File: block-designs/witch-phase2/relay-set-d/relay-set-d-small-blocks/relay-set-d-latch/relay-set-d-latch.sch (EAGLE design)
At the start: 53 parts, among them IC1 74LVC1G125DBV, IC10 741G175, IC11 74LVC1G06DBV, IC12 74LVC1G06DBV, IC13 74LVC1G06DBV, IC14 74LVC1G06DBV, IC15 74LVC1G06DBV, IC2 74LVC1G125DBV, IC3 74LVC1G125DBV, IC4 74LVC1G125DBV, IC5 74LVC1G125DBV, IC6 741G175, IC7 741G175, IC8 741G175, IC9 741G175, Q1 MMBT2907ALT1SMD, Q2 MMBT2907ALT1SMD

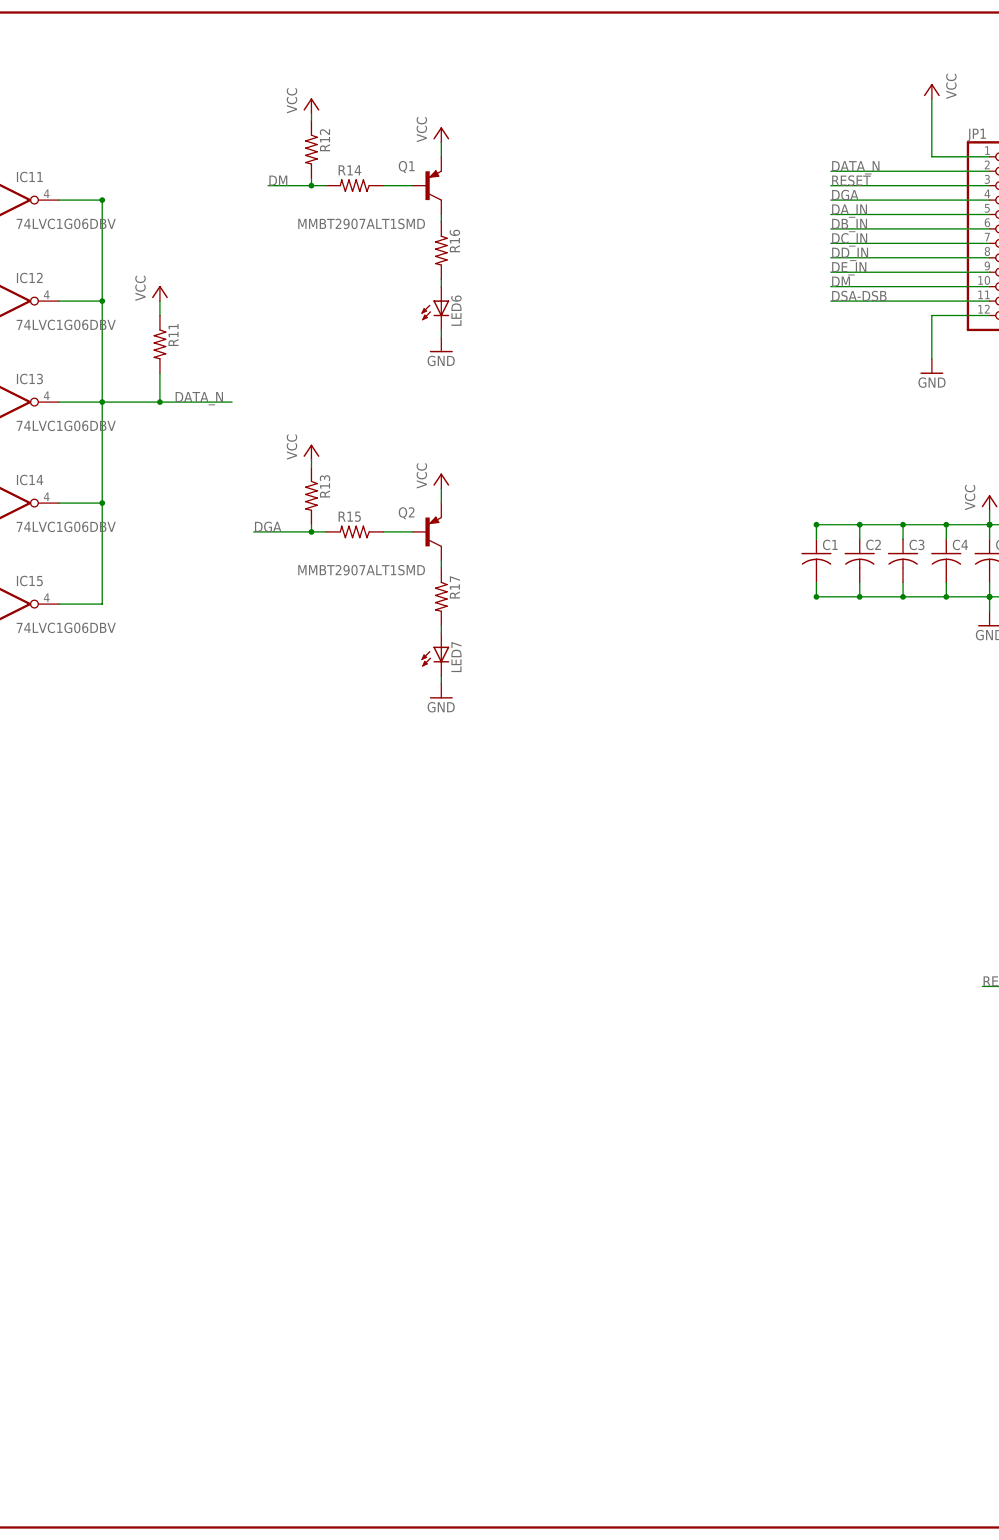
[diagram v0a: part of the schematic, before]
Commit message: add inverting schmitt trigger to valid data detect output
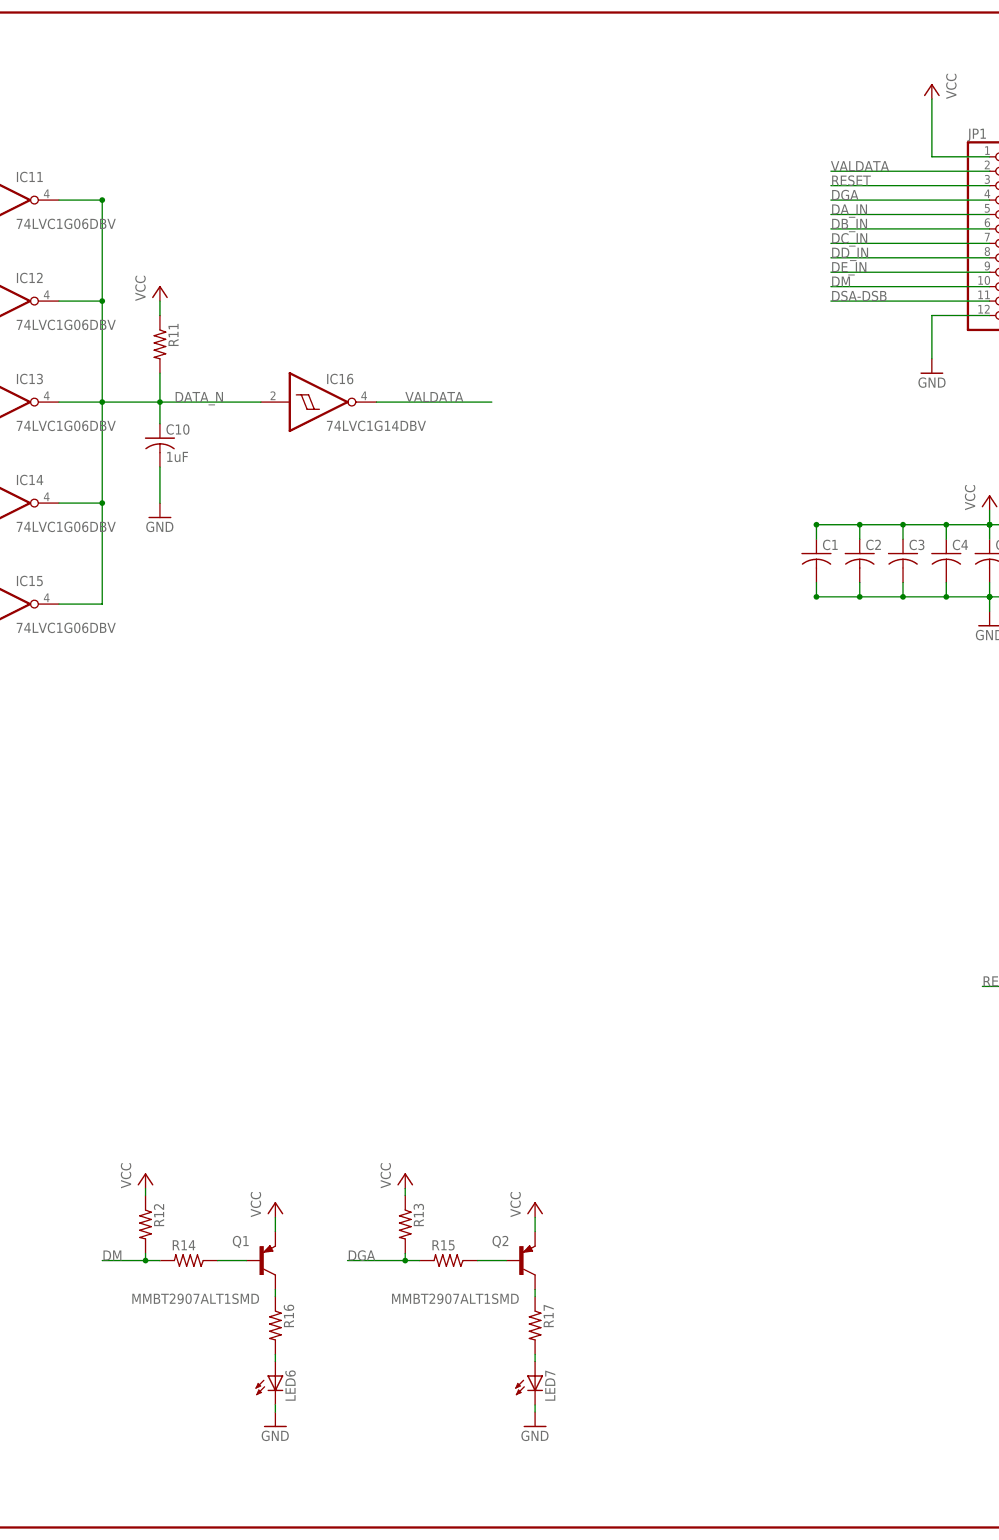
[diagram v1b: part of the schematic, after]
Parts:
- added C10: 1uF, resistor:C-USC0805
- added IC16: 74LVC1G14DBV, 74xx-little-us:74LVC1G14DBV
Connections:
- new net VALDATA: IC16A.O, JP1.2
- net DATA_N: now also C10.1, IC16A.I; no longer JP1.2
- net GND: now also C10.2
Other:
- moved on the sheet: LED6, LED7, Q1, Q2, R12, R13, R14, R15, R16, R17

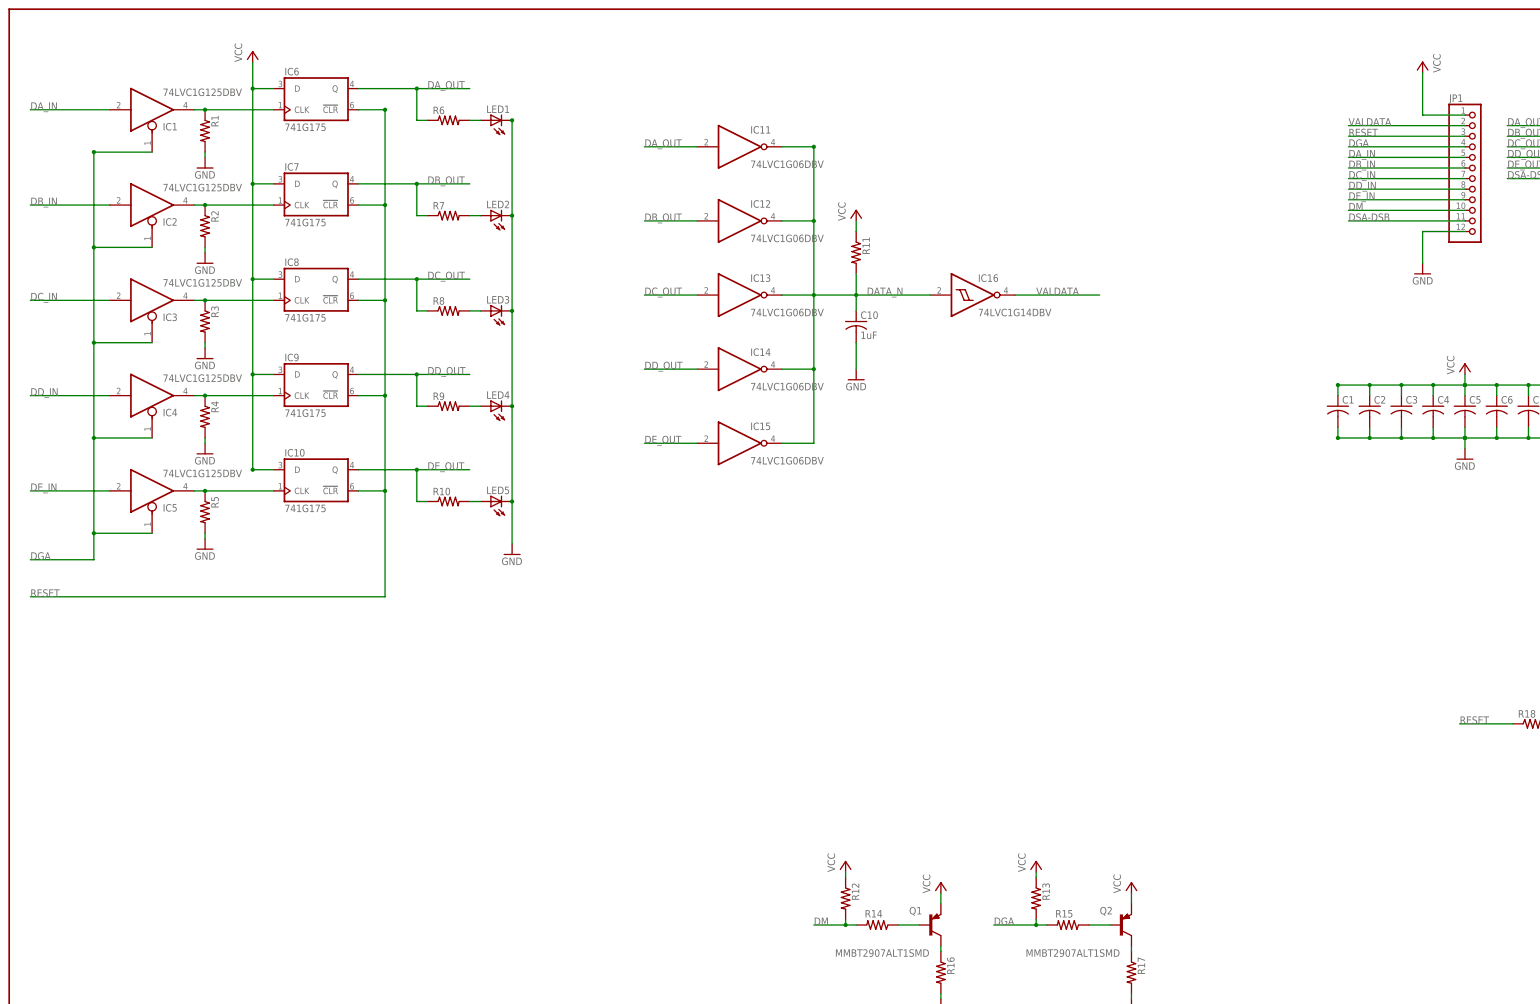
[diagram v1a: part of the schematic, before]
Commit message: add inverting schemitt trigger for enable line and connect valdata led
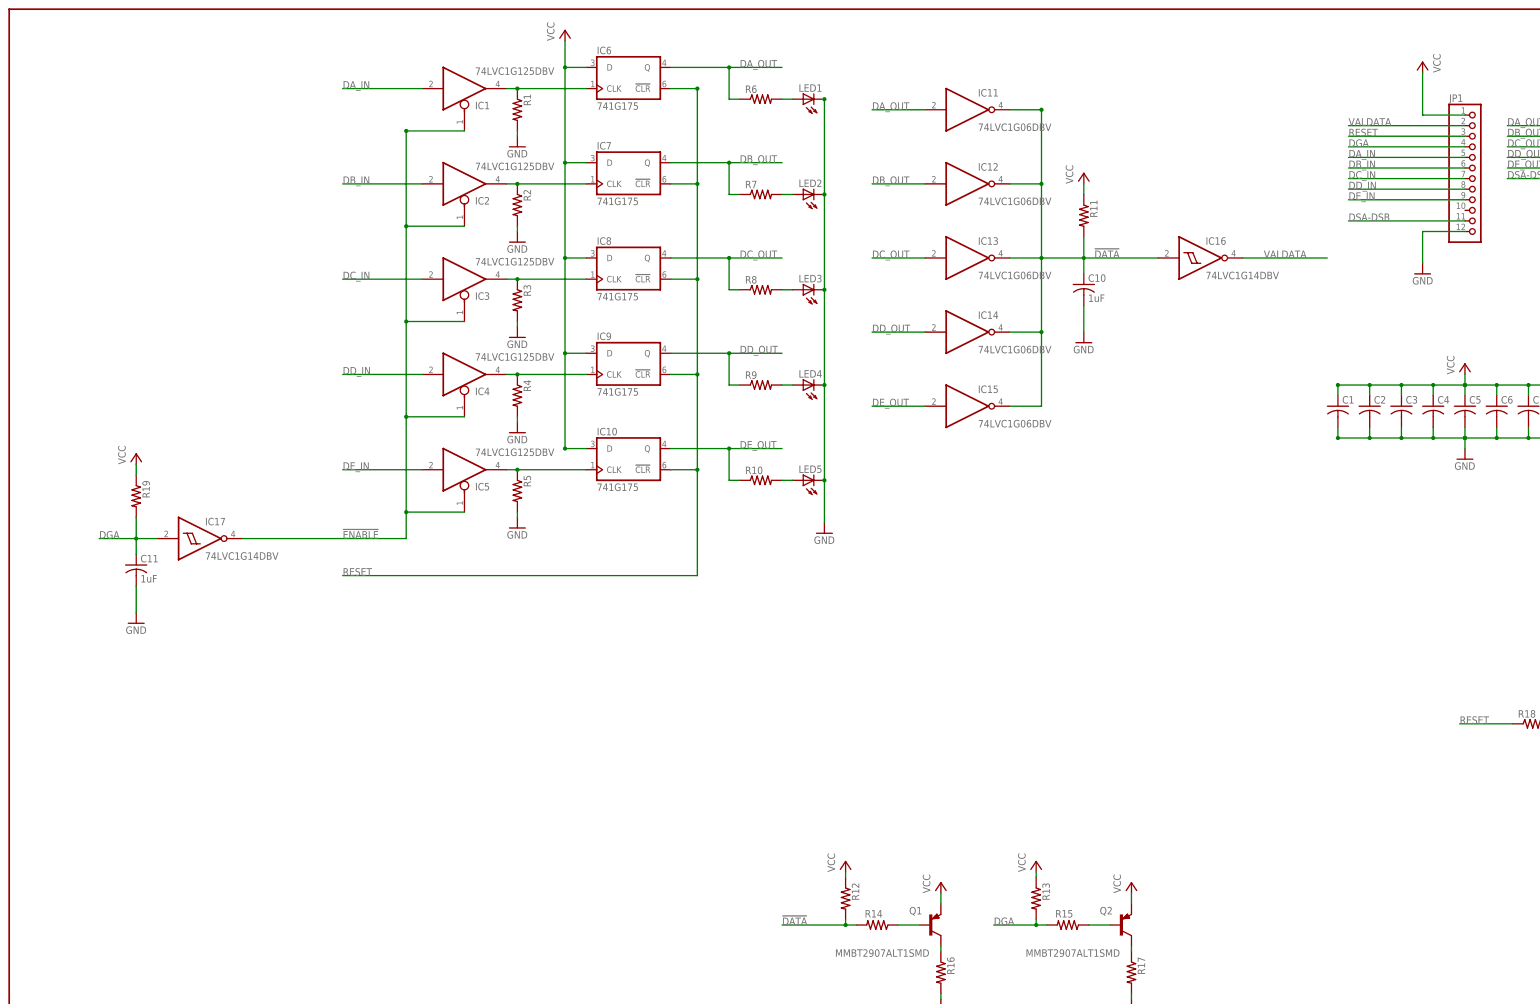
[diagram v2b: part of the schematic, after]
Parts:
- added C11: 1uF, resistor:C-USC0805
- added IC17: 74LVC1G14DBV, 74xx-little-us:74LVC1G14DBV
- added R19: (no value), resistor:R-US_R0805
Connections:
- removed net DATA_N: C10.1, IC11G$1.O, IC12G$1.O, IC13G$1.O, IC14G$1.O, IC15G$1.O, IC16A.I, R11.2
- removed net DM: JP1.10, R12.2, R14.2
- new net !DATA: C10.1, IC11G$1.O, IC12G$1.O, IC13G$1.O, IC14G$1.O, IC15G$1.O, IC16A.I, R11.2, R12.2, R14.2
- new net !ENABLE: IC17A.O, IC1A.OE, IC2A.OE, IC3A.OE, IC4A.OE, IC5A.OE
- net DGA: now also C11.1, IC17A.I, R19.2; no longer IC1A.OE, IC2A.OE, IC3A.OE, IC4A.OE, IC5A.OE
- net GND: now also C11.2
- net VCC: now also R19.1
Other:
- moved on the sheet: C10, IC1, IC10, IC11, IC12, IC13, IC14, IC15, IC16, IC2, IC3, IC4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

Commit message: updated layout for easier interfacing
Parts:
- removed IC13, IC14, IC15: 74LVC1G06DBV, 74xx-little-us:74AUC1G06DBV
- removed IC16: 74LVC1G14DBV, 74xx-little-us:74LVC1G14DBV
- removed R13: (no value), resistor:R-US_R0805
- added D1, D2, D3, D4, D5: MBR0520LT, diode:MBR0520LT
- C10, C11, C5, C6, C7, C8, C9: device resistor:C-USC0805 -> resistor:C-USC0603K
- IC11, IC12: value 74LVC1G06DBV -> 74LVC1G17DBV; device 74xx-little-us:74AUC1G06DBV -> 74xx-little-us:74LVC1G17DBV
- JP1: device pinhead:PINHD-1X12 -> custom-pinhead:PINHD-2X12
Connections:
- removed net !DATA: C10.1, IC11G$1.O, IC12G$1.O, IC13G$1.O, IC14G$1.O, IC15G$1.O, IC16A.I, R11.2, R12.2, R14.2
- removed net DGA: C11.1, IC17A.I, JP1.4, R13.2, R15.2, R19.2
- removed net DSA-DSB: JP1.11, JP2.7
- removed net RESET: IC10G$1.!CLR, IC6G$1.!CLR, IC7G$1.!CLR, IC8G$1.!CLR, IC9G$1.!CLR, JP1.3, R18.1
- new net !CLEAR: IC10G$1.!CLR, IC12G$1.O, IC6G$1.!CLR, IC7G$1.!CLR, IC8G$1.!CLR, IC9G$1.!CLR, R18.1
- new net !RESET: C10.1, IC12G$1.I, JP1.13, JP1.14, R12.2
- new net DATA: D1.C, D2.C, D3.C, D4.C, D5.C, IC11G$1.I, R11.1, R14.2
- new net SELECT: C11.1, IC17A.I, JP1.21, JP1.22, R15.2, R19.2
- net DA_IN: now also JP1.3, JP1.4; no longer JP1.5
- net DA_OUT: now also D1.A; no longer IC11G$1.I
- net DB_IN: now also JP1.5
- net DB_OUT: now also D2.A; no longer IC12G$1.I
- net DC_IN: now also JP1.8
- net DC_OUT: now also D3.A; no longer IC13G$1.I
- net DD_IN: now also JP1.10, JP1.9; no longer JP1.8
- net DD_OUT: now also D4.A; no longer IC14G$1.I
- net DE_IN: now also JP1.11, JP1.12; no longer JP1.9
- net DE_OUT: now also D5.A; no longer IC15G$1.I
- net GND: now also JP1.15, JP1.16, JP1.23, JP1.24, R11.2; no longer JP1.12
- net VALDATA: now also IC11G$1.O, JP1.19, JP1.20; no longer IC16A.O, JP1.2
- net VCC: now also JP1.17, JP1.18, JP1.2; no longer R11.1, R13.1
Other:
- moved on the sheet: C1, C10, C11, C2, C3, C4, C5, C6, C7, C8, C9, IC1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
